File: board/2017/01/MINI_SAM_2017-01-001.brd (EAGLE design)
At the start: 24.1 x 39.2 mm, 36 parts, among them IC2 USBLC6-2, J1 MOLEX_47346-100147346, J2 CORTEX_DEBUGPTH, SW1 KMS_SWITCHKMS, SW2 KMS_SWITCHKMS, U1 SAMD21ETQFP, Y1 32.768kHz 7pF

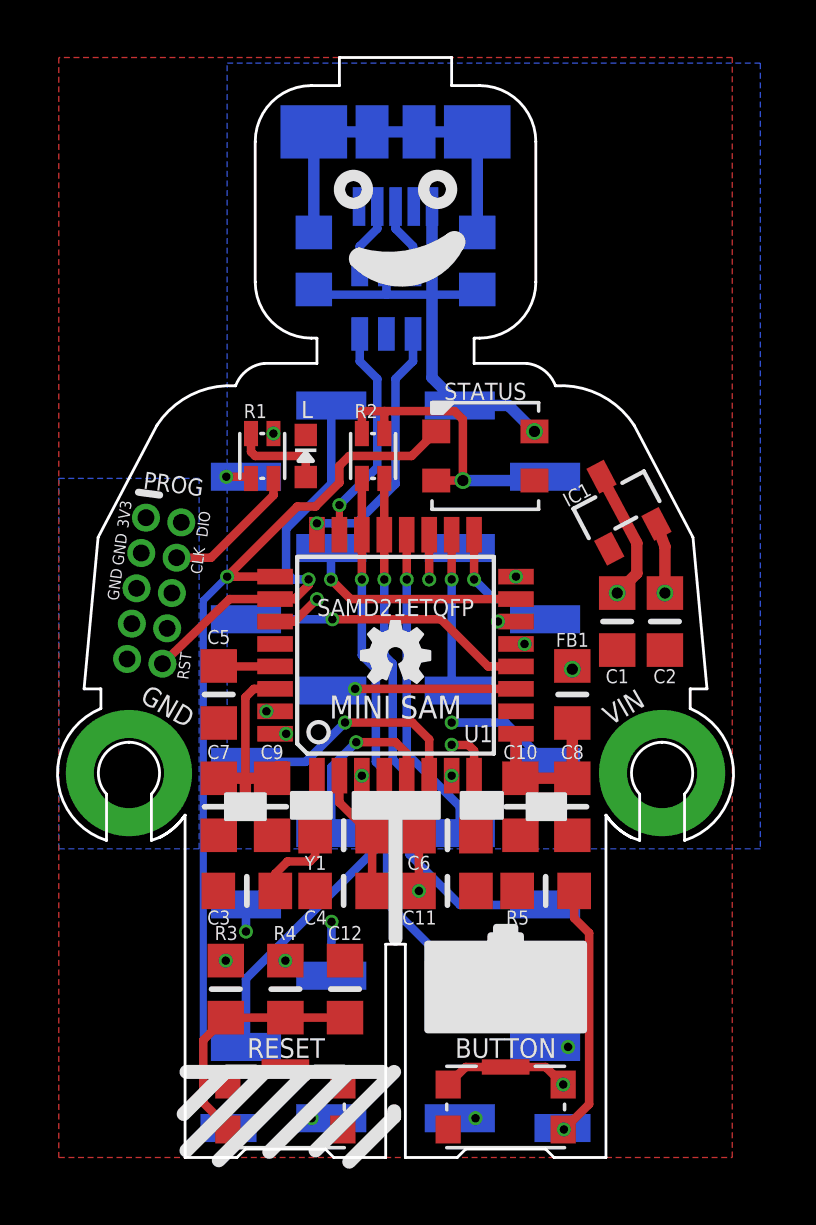
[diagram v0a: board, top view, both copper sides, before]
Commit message: Updated Internal Layer
Updated one of the internal layers to include a ground plane for better grounding.
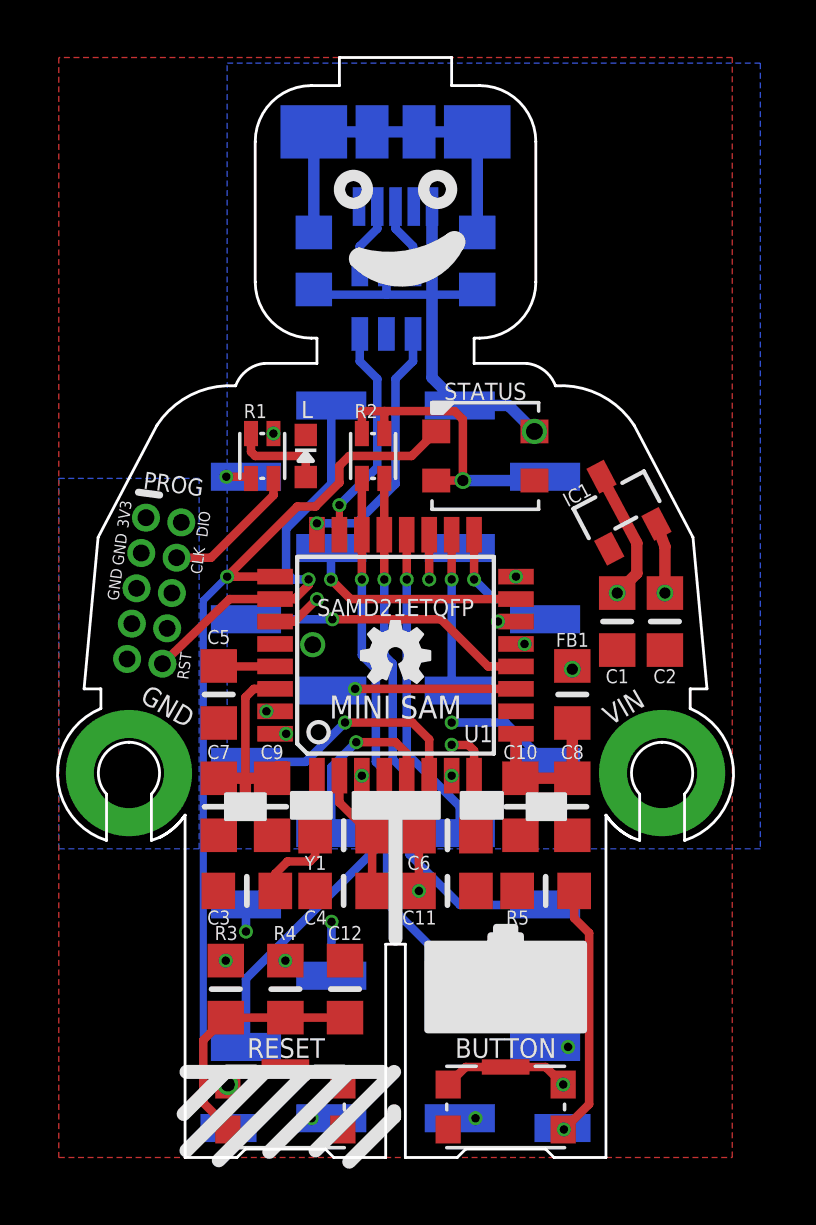
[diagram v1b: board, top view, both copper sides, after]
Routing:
- net GND: vias 2 -> 4
- added copper zone on layer 2, net GND
